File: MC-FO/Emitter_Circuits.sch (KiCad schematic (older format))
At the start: 8 parts, among them U7 74ACT08SCX, U8 IFE98

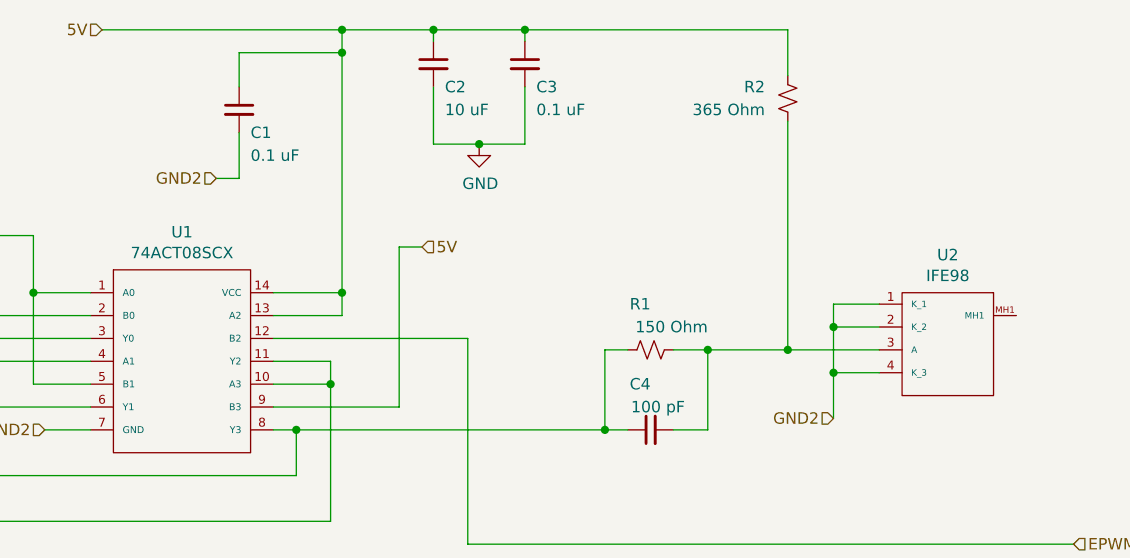
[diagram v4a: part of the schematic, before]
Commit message: unpopulated cap after voltage regulators
and changed reference designator numbering scheme
and moved the or gate that sends 3.3 V to comparator in detector ckt
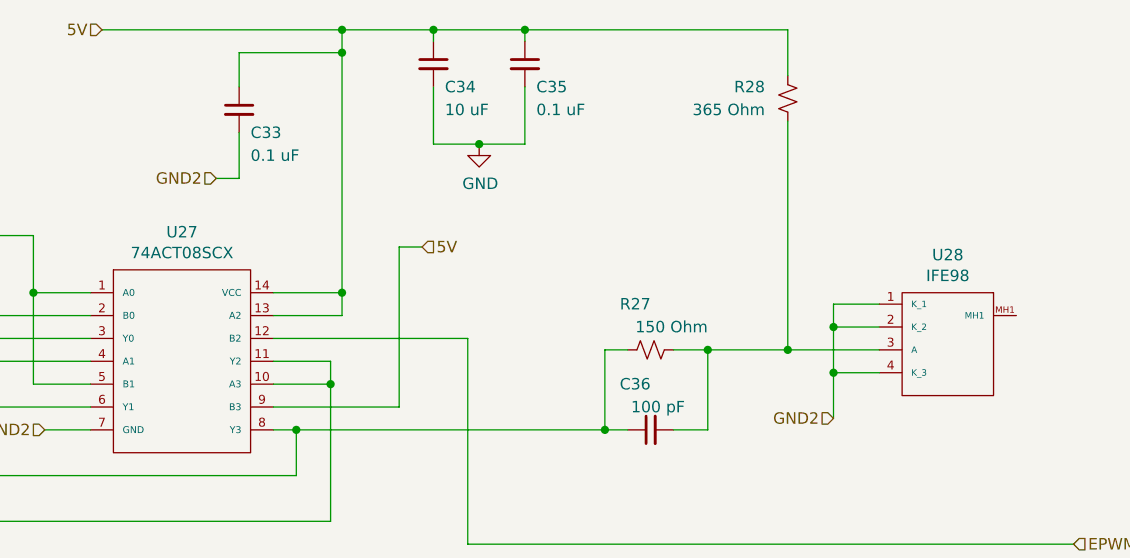
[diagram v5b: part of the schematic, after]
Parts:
- renumbered C13 to C33, C14 to C34, C15 to C35, C16 to C36, R7 to R27, R8 to R28, U7 to U27, U8 to U28
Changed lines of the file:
@@
 $Descr A4 11693 8268
 encoding utf-8
-Sheet 2 11
+Sheet 5 11
 Title ""
 Date ""
@@
 Emitter CKT
 $Comp
-L Device:R_Small_US R7
+L Device:R_Small_US R27
 U 1 1 617428A7
 P 6700 4400
-AR Path="/61717EAF/617428A7" Ref="R7"  Part="1"
-AR Path="/617509F7/617428A7" Ref="R9"  Part="1"
-AR Path="/61750A2A/617428A7" Ref="R11"  Part="1"
-AR Path="/6176CA10/617428A7" Ref="R1"  Part="1"
-AR Path="/6176CA81/617428A7" Ref="R3"  Part="1"
-AR Path="/6176CAE4/617428A7" Ref="R5"  Part="1"
-F 0 "R1" V 6900 4400 50  0000 L CNN
+AR Path="/61717EAF/617428A7" Ref="R27"  Part="1"
+AR Path="/617509F7/617428A7" Ref="R41"  Part="1"
+AR Path="/61750A2A/617428A7" Ref="R61"  Part="1"
+AR Path="/6176CA10/617428A7" Ref="R81"  Part="1"
+AR Path="/6176CA81/617428A7" Ref="R101"  Part="1"
+AR Path="/6176CAE4/617428A7" Ref="R121"  Part="1"
+F 0 "R27" V 6900 4400 50  0000 L CNN
 F 1 "150 Ohm" V 6800 4150 50  0000 L CNN
 F 2 "Resistor_SMD:R_0603_1608Metric" H 6700 4400 50  0001 C CNN
@@
 $EndComp
 $Comp
-L Device:C_Small C16
+L Device:C_Small C36
 U 1 1 61748E58
 P 6700 4750
-AR Path="/61717EAF/61748E58" Ref="C16"  Part="1"
-AR Path="/617509F7/61748E58" Ref="C20"  Part="1"
-AR Path="/61750A2A/61748E58" Ref="C24"  Part="1"
-AR Path="/6176CA10/61748E58" Ref="C4"  Part="1"
-AR Path="/6176CA81/61748E58" Ref="C8"  Part="1"
-AR Path="/6176CAE4/61748E58" Ref="C12"  Part="1"
-F 0 "C4" V 6900 4750 50  0000 L CNN
+AR Path="/61717EAF/61748E58" Ref="C36"  Part="1"
+AR Path="/617509F7/61748E58" Ref="C44"  Part="1"
+AR Path="/61750A2A/61748E58" Ref="C64"  Part="1"
+AR Path="/6176CA10/61748E58" Ref="C84"  Part="1"
+AR Path="/6176CA81/61748E58" Ref="C104"  Part="1"
+AR Path="/6176CAE4/61748E58" Ref="C124"  Part="1"
+F 0 "C36" V 6900 4750 50  0000 L CNN
 F 1 "100 pF" V 6800 4600 50  0000 L CNN
 F 2 "Capacitor_SMD:C_0603_1608Metric" H 6700 4750 50  0001 C CNN
@@
 	6950 4400 6800 4400
 $Comp
-L Device:R_Small_US R8
+L Device:R_Small_US R28
 U 1 1 6178E7F7
 P 7300 3300
-AR Path="/61717EAF/6178E7F7" Ref="R8"  Part="1"
-AR Path="/617509F7/6178E7F7" Ref="R10"  Part="1"
-AR Path="/61750A2A/6178E7F7" Ref="R12"  Part="1"
-AR Path="/6176CA10/6178E7F7" Ref="R2"  Part="1"
-AR Path="/6176CA81/6178E7F7" Ref="R4"  Part="1"
-AR Path="/6176CAE4/6178E7F7" Ref="R6"  Part="1"
-F 0 "R2" H 7400 3250 50  0000 L CNN
+AR Path="/61717EAF/6178E7F7" Ref="R28"  Part="1"
+AR Path="/617509F7/6178E7F7" Ref="R42"  Part="1"
+AR Path="/61750A2A/6178E7F7" Ref="R62"  Part="1"
+AR Path="/6176CA10/6178E7F7" Ref="R82"  Part="1"
+AR Path="/6176CA81/6178E7F7" Ref="R102"  Part="1"
+AR Path="/6176CAE4/6178E7F7" Ref="R122"  Part="1"
+F 0 "R28" H 7400 3250 50  0000 L CNN
 F 1 "365 Ohm" H 7400 3350 50  0000 L CNN
 F 2 "Resistor_SMD:R_0603_1608Metric" H 7300 3300 50  0001 C CNN
@@
 	4900 3100 4900 3250
 $Comp
-L Device:C_Small C13
+L Device:C_Small C33
 U 1 1 6171F0C9
 P 4900 3350
-AR Path="/61717EAF/6171F0C9" Ref="C13"  Part="1"
-AR Path="/617509F7/6171F0C9" Ref="C17"  Part="1"
-AR Path="/61750A2A/6171F0C9" Ref="C21"  Part="1"
-AR Path="/6176CA10/6171F0C9" Ref="C1"  Part="1"
-AR Path="/6176CA81/6171F0C9" Ref="C5"  Part="1"
-AR Path="/6176CAE4/6171F0C9" Ref="C9"  Part="1"
-F 0 "C1" H 4950 3250 50  0000 L CNN
+AR Path="/61717EAF/6171F0C9" Ref="C33"  Part="1"
+AR Path="/617509F7/6171F0C9" Ref="C41"  Part="1"
+AR Path="/61750A2A/6171F0C9" Ref="C61"  Part="1"
+AR Path="/6176CA10/6171F0C9" Ref="C81"  Part="1"
+AR Path="/6176CA81/6171F0C9" Ref="C101"  Part="1"
+AR Path="/6176CAE4/6171F0C9" Ref="C121"  Part="1"
+F 0 "C33" H 4950 3250 50  0000 L CNN
 F 1 "0.1 uF" H 4950 3150 50  0000 L CNN
 F 2 "Capacitor_SMD:C_0603_1608Metric" H 4900 3350 50  0001 C CNN
@@
 	5950 3500 5750 3500
 $Comp
-L power:GND #PWR07
+L power:GND #PWR027
 U 1 1 61735A2B
 P 5950 3500
-AR Path="/61717EAF/61735A2B" Ref="#PWR07"  Part="1"
-AR Path="/617509F7/61735A2B" Ref="#PWR08"  Part="1"
-AR Path="/61750A2A/61735A2B" Ref="#PWR09"  Part="1"
-AR Path="/6176CA10/61735A2B" Ref="#PWR04"  Part="1"
-AR Path="/6176CA81/61735A2B" Ref="#PWR05"  Part="1"
-AR Path="/6176CAE4/61735A2B" Ref="#PWR06"  Part="1"
-F 0 "#PWR04" H 5950 3250 50  0001 C CNN
+AR Path="/61717EAF/61735A2B" Ref="#PWR027"  Part="1"
+AR Path="/617509F7/61735A2B" Ref="#PWR041"  Part="1"
+AR Path="/61750A2A/61735A2B" Ref="#PWR061"  Part="1"
+AR Path="/6176CA10/61735A2B" Ref="#PWR081"  Part="1"
+AR Path="/6176CA81/61735A2B" Ref="#PWR0101"  Part="1"
+AR Path="/6176CAE4/61735A2B" Ref="#PWR0121"  Part="1"
+F 0 "#PWR027" H 5950 3250 50  0001 C CNN
 F 1 "GND" H 5955 3327 50  0000 C CNN
 F 2 "" H 5950 3500 50  0001 C CNN
@@
 $EndComp
 $Comp
-L Device:C_Small C15
+L Device:C_Small C35
 U 1 1 61733718
 P 6150 3150
-AR Path="/61717EAF/61733718" Ref="C15"  Part="1"
-AR Path="/617509F7/61733718" Ref="C19"  Part="1"
-AR Path="/61750A2A/61733718" Ref="C23"  Part="1"
-AR Path="/6176CA10/61733718" Ref="C3"  Part="1"
-AR Path="/6176CA81/61733718" Ref="C7"  Part="1"
-AR Path="/6176CAE4/61733718" Ref="C11"  Part="1"
-F 0 "C3" H 6200 3050 50  0000 L CNN
+AR Path="/61717EAF/61733718" Ref="C35"  Part="1"
+AR Path="/617509F7/61733718" Ref="C43"  Part="1"
+AR Path="/61750A2A/61733718" Ref="C63"  Part="1"
+AR Path="/6176CA10/61733718" Ref="C83"  Part="1"
+AR Path="/6176CA81/61733718" Ref="C103"  Part="1"
+AR Path="/6176CAE4/61733718" Ref="C123"  Part="1"
+F 0 "C35" H 6200 3050 50  0000 L CNN
 F 1 "0.1 uF" H 6200 2950 50  0000 L CNN
 F 2 "Capacitor_SMD:C_0603_1608Metric" H 6150 3150 50  0001 C CNN
@@
 	5750 3000 5750 3050
 $Comp
-L Device:C_Small C14
+L Device:C_Small C34
 U 1 1 61730A88
 P 5750 3150
-AR Path="/61717EAF/61730A88" Ref="C14"  Part="1"
-AR Path="/617509F7/61730A88" Ref="C18"  Part="1"
-AR Path="/61750A2A/61730A88" Ref="C22"  Part="1"
-AR Path="/6176CA10/61730A88" Ref="C2"  Part="1"
-AR Path="/6176CA81/61730A88" Ref="C6"  Part="1"
-AR Path="/6176CAE4/61730A88" Ref="C10"  Part="1"
-F 0 "C2" H 5800 3050 50  0000 L CNN
+AR Path="/61717EAF/61730A88" Ref="C34"  Part="1"
+AR Path="/617509F7/61730A88" Ref="C42"  Part="1"
+AR Path="/61750A2A/61730A88" Ref="C62"  Part="1"
+AR Path="/6176CA10/61730A88" Ref="C82"  Part="1"
+AR Path="/6176CA81/61730A88" Ref="C102"  Part="1"
+AR Path="/6176CAE4/61730A88" Ref="C122"  Part="1"
+F 0 "C34" H 5800 3050 50  0000 L CNN
 F 1 "10 uF" H 5800 2950 50  0000 L CNN
 F 2 "Capacitor_SMD:C_0603_1608Metric" H 5750 3150 50  0001 C CNN
@@
 	4050 4750 4250 4750
 $Comp
-L Existing_IC_Models:74ACT08SCX U7
+L Existing_IC_Models:74ACT08SCX U27
 U 1 1 61804FDE
 P 4650 4000
-AR Path="/61717EAF/61804FDE" Ref="U7"  Part="1"
-AR Path="/617509F7/61804FDE" Ref="U9"  Part="1"
-AR Path="/61750A2A/61804FDE" Ref="U11"  Part="1"
-AR Path="/6176CA10/61804FDE" Ref="U1"  Part="1"
-AR Path="/6176CA81/61804FDE" Ref="U3"  Part="1"
-AR Path="/6176CAE4/61804FDE" Ref="U5"  Part="1"
-F 0 "U1" H 4650 4115 50  0000 C CNN
+AR Path="/61717EAF/61804FDE" Ref="U27"  Part="1"
+AR Path="/617509F7/61804FDE" Ref="U41"  Part="1"
+AR Path="/61750A2A/61804FDE" Ref="U61"  Part="1"
+AR Path="/6176CA10/61804FDE" Ref="U81"  Part="1"
+AR Path="/6176CA81/61804FDE" Ref="U101"  Part="1"
+AR Path="/6176CAE4/61804FDE" Ref="U121"  Part="1"
+F 0 "U27" H 4650 4115 50  0000 C CNN
 F 1 "74ACT08SCX" H 4650 4024 50  0000 C CNN
 F 2 "Package_SO:SOIC-14_3.9x8.7mm_P1.27mm" H 4650 4000 50  0001 C CNN
@@
 	4900 3650 4800 3650
 $Comp
-L Existing_IC_Models:IFE98 U8
+L Existing_IC_Models:IFE98 U28
 U 1 1 61778B54
 P 8000 4100
-AR Path="/61717EAF/61778B54" Ref="U8"  Part="1"
-AR Path="/61750A2A/61778B54" Ref="U12"  Part="1"
-AR Path="/6176CA10/61778B54" Ref="U2"  Part="1"
-AR Path="/6176CA81/61778B54" Ref="U4"  Part="1"
-AR Path="/6176CAE4/61778B54" Ref="U6"  Part="1"
-AR Path="/617509F7/61778B54" Ref="U10"  Part="1"
-F 0 "U2" H 8000 4215 50  0000 C CNN
+AR Path="/61717EAF/61778B54" Ref="U28"  Part="1"
+AR Path="/61750A2A/61778B54" Ref="U62"  Part="1"
+AR Path="/6176CA10/61778B54" Ref="U82"  Part="1"
+AR Path="/6176CA81/61778B54" Ref="U102"  Part="1"
+AR Path="/6176CAE4/61778B54" Ref="U122"  Part="1"
+AR Path="/617509F7/61778B54" Ref="U42"  Part="1"
+F 0 "U28" H 8000 4215 50  0000 C CNN
 F 1 "IFE98" H 8000 4124 50  0000 C CNN
 F 2 "Footprints_MC-FO:IFE98" H 8000 4100 50  0001 C CNN

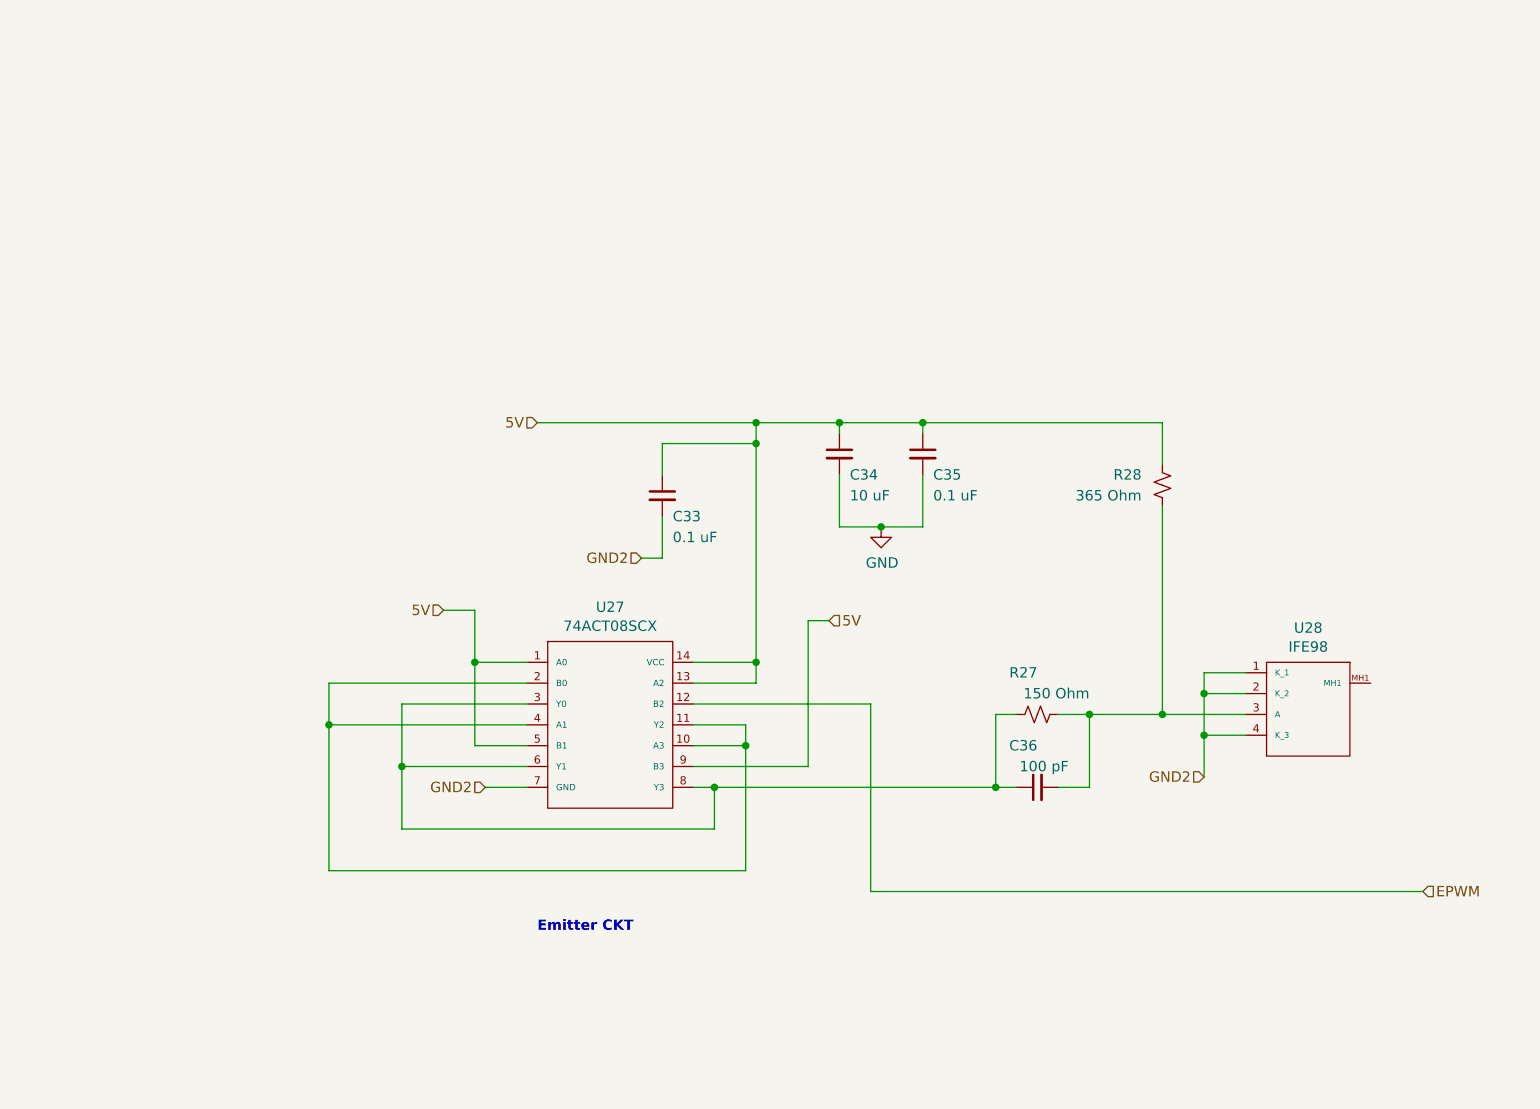
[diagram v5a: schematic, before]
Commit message: Fixed file hierarchy
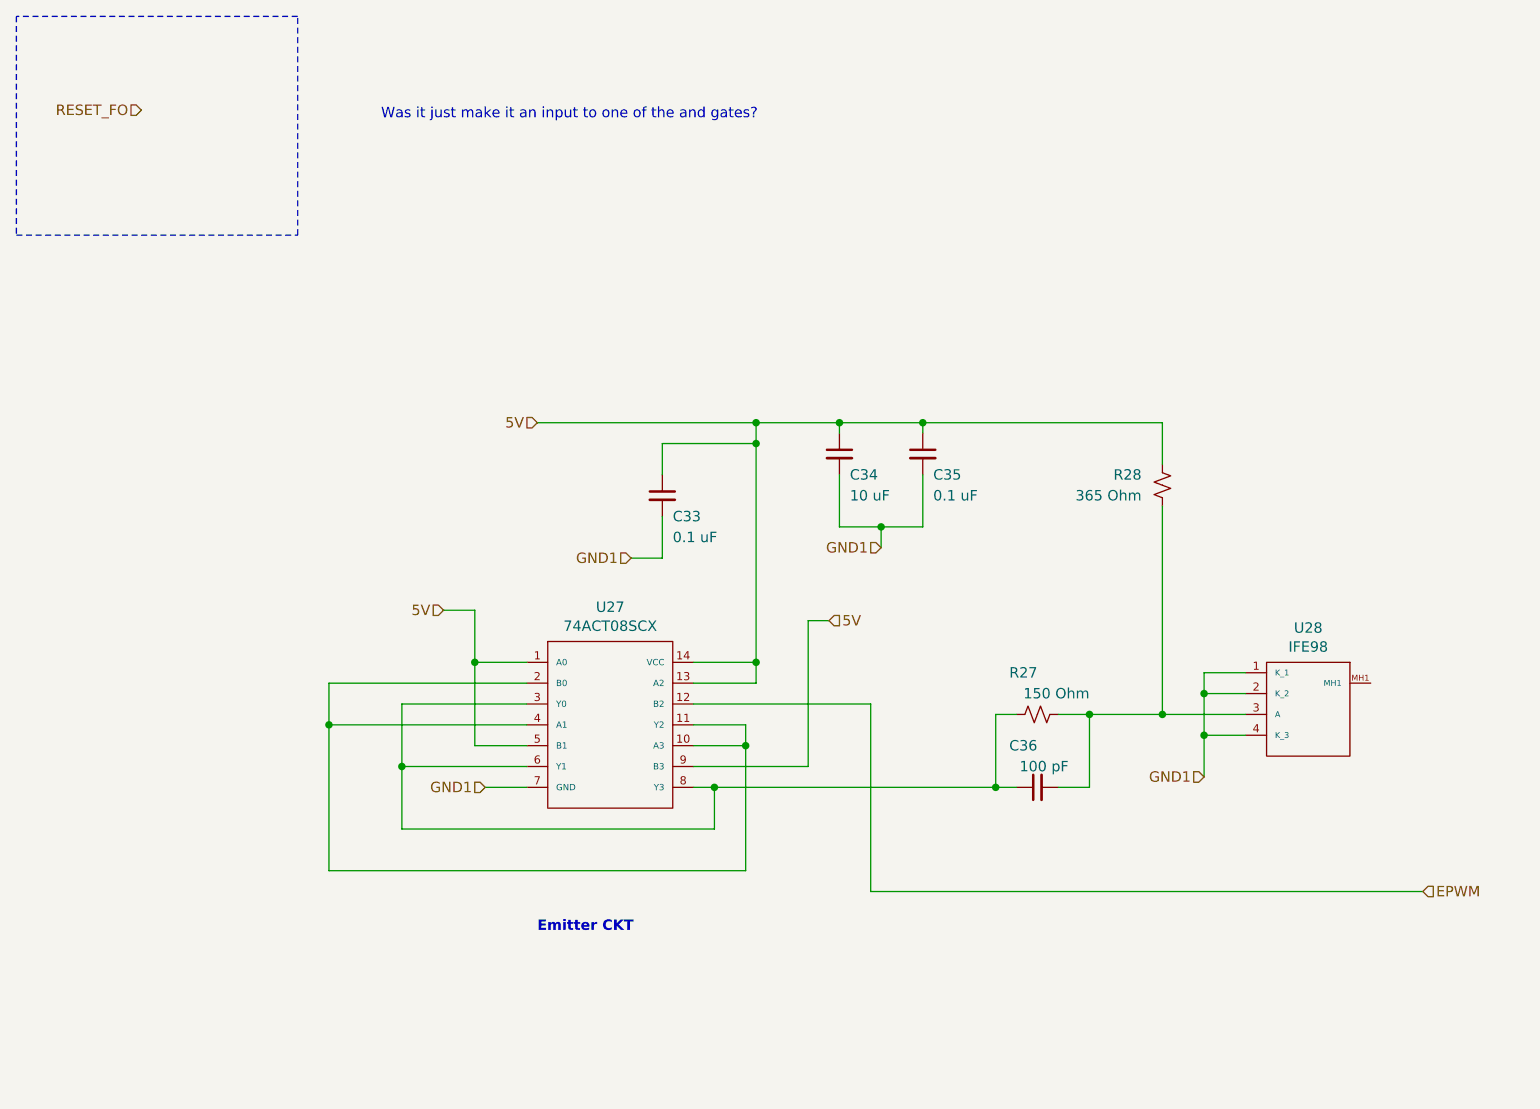
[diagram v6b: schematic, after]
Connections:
- net GND2 is gone; now on net GND1: C33.2, U27.7 (GND), U28.1 (K_1), U28.2 (K_2), U28.4 (K_3)
- net GND renamed GND1
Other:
- note added: "Was it just make it an input to one of the and gates?"
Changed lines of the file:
@@
 $Descr A4 11693 8268
 encoding utf-8
-Sheet 5 11
+Sheet 4 11
 Title ""
 Date ""
@@
 Connection ~ 5750 3000
 Wire Wire Line
-	5950 3500 6150 3500
-Wire Wire Line
 	6150 3050 6150 3000
-Connection ~ 5950 3500
 Wire Wire Line
 	6150 3500 6150 3250
 Wire Wire Line
 	5750 3500 5750 3250
-Wire Wire Line
-	5950 3500 5750 3500
-$Comp
-L power:GND #PWR027
-U 1 1 61735A2B
-P 5950 3500
-AR Path="/61717EAF/61735A2B" Ref="#PWR027"  Part="1"
-AR Path="/617509F7/61735A2B" Ref="#PWR041"  Part="1"
-AR Path="/61750A2A/61735A2B" Ref="#PWR061"  Part="1"
-AR Path="/6176CA10/61735A2B" Ref="#PWR081"  Part="1"
-AR Path="/6176CA81/61735A2B" Ref="#PWR0101"  Part="1"
-AR Path="/6176CAE4/61735A2B" Ref="#PWR0121"  Part="1"
-F 0 "#PWR027" H 5950 3250 50  0001 C CNN
-F 1 "GND" H 5955 3327 50  0000 C CNN
-F 2 "" H 5950 3500 50  0001 C CNN
-F 3 "" H 5950 3500 50  0001 C CNN
-	1    5950 3500
-	1    0    0    -1
-$EndComp
 $Comp
 L Device:C_Small C35
@@
 5V
 Text HLabel 7500 4700 0    50   Input ~ 0
-GND2
-Text HLabel 4800 3650 0    50   Input ~ 0
-GND2
+GND1
 Wire Wire Line
 	4300 3000 5350 3000
@@
 $EndComp
 Text HLabel 4050 4750 0    50   Input ~ 0
-GND2
+GND1
 Wire Wire Line
 	5350 3100 5350 4150
@@
 Wire Wire Line
 	5050 4350 5900 4350
-Wire Wire Line
-	4900 3650 4800 3650
 $Comp
 L Existing_IC_Models:IFE98 U28
@@
 	3650 4350 3650 4650
 Connection ~ 3650 4650
+Wire Notes Line
+	1800 2100 3150 2100
+Wire Notes Line
+	3150 2100 3150 1050
+Wire Notes Line
+	3150 1050 1800 1050
+Wire Notes Line
+	1800 1050 1800 2100
+Text HLabel 2400 1500 0    50   Input ~ 0
+RESET_FO
+Wire Wire Line
+	5750 3500 5950 3500
+Wire Wire Line
+	5950 3500 5950 3600
+Connection ~ 5950 3500
+Wire Wire Line
+	5950 3500 6150 3500
+Text HLabel 5950 3600 0    50   Input ~ 0
+GND1
+Text HLabel 4750 3650 0    50   Input ~ 0
+GND1
+Wire Wire Line
+	4750 3650 4900 3650
+Text Notes 3550 1550 0    50   ~ 0
+Was it just make it an input to one of the and gates?
 $EndSCHEMATC
